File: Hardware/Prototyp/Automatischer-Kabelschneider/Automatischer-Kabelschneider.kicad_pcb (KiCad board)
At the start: 4 copper layers, 160 x 100 mm, 141 parts, among them J1 USB_C_Receptacle_USB2.0_16P, J10 Conn_02x05_Odd_Even, J11 Conn_02x05_Odd_Even, J12 Conn_01x05, J2 Conn_01x04, J3 Conn_01x04, J4 Conn_01x02, J5 Conn_02x05_Odd_Even, J6 Conn_01x04, J7 Conn_02x05_Odd_Even, J8 Conn_02x05_Odd_Even, J9 Conn_02x05_Odd_Even, Q1 IRF540N, Q2 IRF540N, Q3 Q_NMOS_GSD, Q4 Q_NMOS_GSD, Q5 Q_NMOS_GSD, Q6 Q_NMOS_GSD, SW1 SW_Push, SW2 SW_Push, SW3 SW_Push, U1 TVS220x, U2 TVS220x, U3 CYPD3177-24LQ, U4 AP63203WU, U5 AP63205WU, U6 TMC2209_SILENTSTEPSTICK, U7 ESP32-S3-WROOM-2, U8 TMC2209_SILENTSTEPSTICK, U9 ATmega2560-16A, Y1 16M

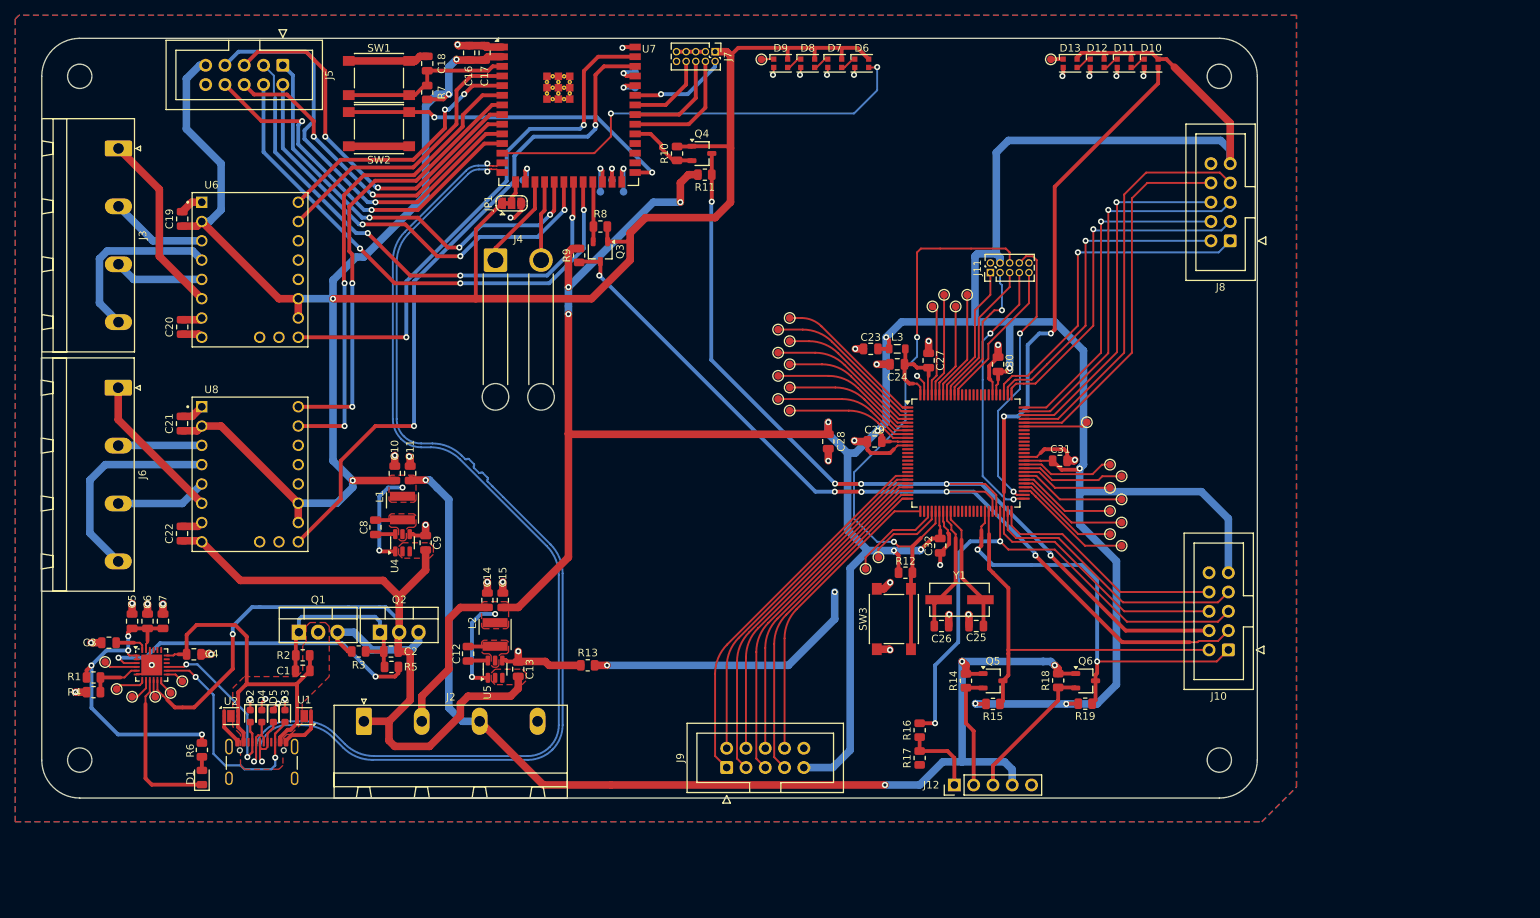
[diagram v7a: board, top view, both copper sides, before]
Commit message: PCB no errors
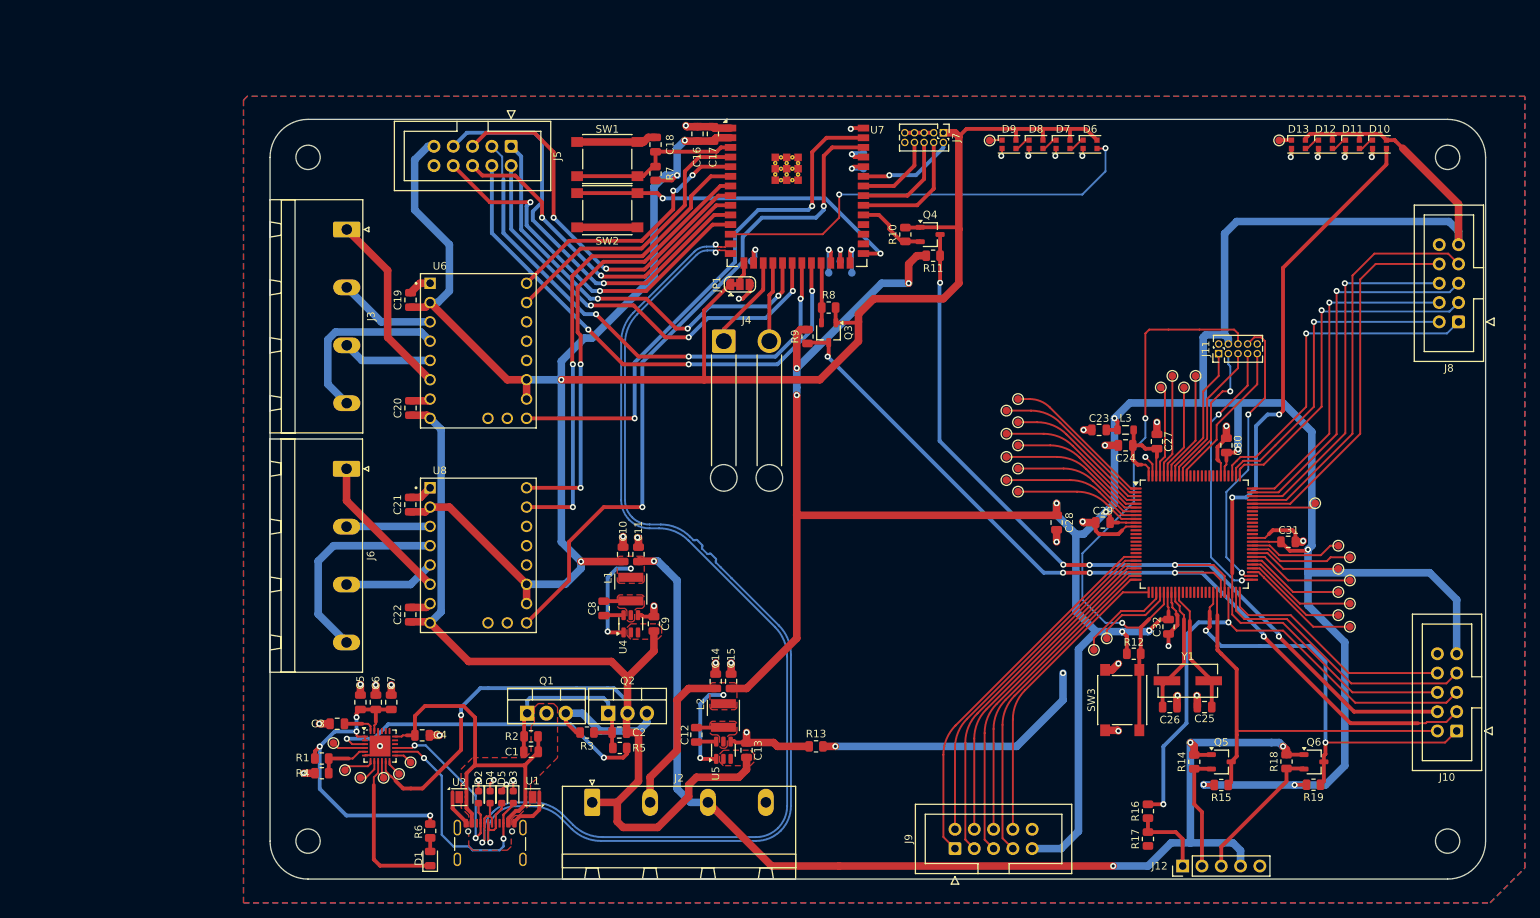
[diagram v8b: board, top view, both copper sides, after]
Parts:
- moved C24 31.9 mm to (181.7, 93.7)
- moved C25 31.9 mm to (192.1, 128.2)
- moved C26 31.9 mm to (187.5, 128.2)
- moved C27 31.9 mm to (185.8, 93.2)
- moved C30 31.9 mm to (195.0, 93.7)
- moved C32 31.9 mm to (187.4, 117.6)
- moved J9 31.9 mm to (159.3, 146.8)
- moved L3 31.9 mm to (181.7, 91.7)
- moved Q6 31.9 mm to (206.5, 135.4)
- moved TP14 31.9 mm to (211.2, 117.6)
- moved TP15 31.9 mm to (209.7, 116.1)
- moved TP16 31.9 mm to (211.2, 114.5)
- moved TP17 31.9 mm to (209.7, 113.0)
- moved TP18 31.9 mm to (211.2, 111.5)
- moved TP19 31.9 mm to (209.7, 110.0)
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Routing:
- net +20V: track 134.9 -> 163.0 mm
